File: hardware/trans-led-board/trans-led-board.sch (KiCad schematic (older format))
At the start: 4 parts, among them J1 Conn_01x02

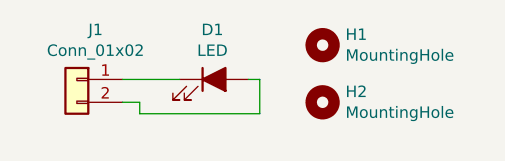
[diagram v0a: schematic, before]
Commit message: Updated transmission LED board design
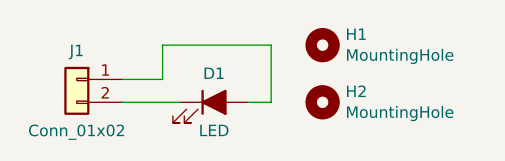
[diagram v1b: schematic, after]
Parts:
- J1: footprint Connector_Wire:SolderWire-0.5sqmm_1x02_P4.6mm_D0.9mm_OD2.1mm -> Connector_JST:JST_SH_SM02B-SRSS-TB_1x02-1MP_P1.00mm_Horizontal; Description (none) -> CONN HEADER SMD R/A 2POS 1MM; Manufacturer (none) -> JST Sales America Inc.; Manufacturer PN (none) -> SM02B-SRSS-TB(LF)(SN); Supplier (none) -> TLC; Supplier PN (none) -> SM02B-SRSS-TB(LF)(SN)
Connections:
- net at D1.1 (K): now also J1.2 (Pin_2); no longer J1.1 (Pin_1)
- net at D1.2 (A): now also J1.1 (Pin_1); no longer J1.2 (Pin_2)
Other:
- moved on the sheet: D1
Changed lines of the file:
@@
 L Device:LED_ALT D1
 U 1 1 609352D1
-P 2575 2050
-F 0 "D1" H 2568 2267 50  0000 C CNN
-F 1 "LED" H 2568 2176 50  0000 C CNN
-F 2 "lib_fp:LED_WL-SWTP-3022" H 2575 2050 50  0001 C CNN
-F 3 "https://katalog.we-online.de/led/datasheet/158302250.pdf" H 2575 2050 50  0001 C CNN
-F 4 "LED WL-SWTP COOL WHT 5000K 2SMD" H 2575 2050 50  0001 C CNN "Description"
-F 5 "Würth Elektronik" H 2575 2050 50  0001 C CNN "Manufacturer"
-F 6 "158302250" H 2575 2050 50  0001 C CNN "Manufacturer PN"
-F 7 "Digi-Key" H 2575 2050 50  0001 C CNN "Supplier"
-F 8 "732-5666-1-ND" H 2575 2050 50  0001 C CNN "Supplier PN"
-	1    2575 2050
+P 2575 2150
+F 0 "D1" H 2575 2275 50  0000 C CNN
+F 1 "LED" H 2575 2025 50  0000 C CNN
+F 2 "lib_fp:LED_WL-SWTP-3022" H 2575 2150 50  0001 C CNN
+F 3 "https://katalog.we-online.de/led/datasheet/158302250.pdf" H 2575 2150 50  0001 C CNN
+F 4 "LED WL-SWTP COOL WHT 5000K 2SMD" H 2575 2150 50  0001 C CNN "Description"
+F 5 "Würth Elektronik" H 2575 2150 50  0001 C CNN "Manufacturer"
+F 6 "158302250" H 2575 2150 50  0001 C CNN "Manufacturer PN"
+F 7 "Digi-Key" H 2575 2150 50  0001 C CNN "Supplier"
+F 8 "732-5666-1-ND" H 2575 2150 50  0001 C CNN "Supplier PN"
+	1    2575 2150
 	1    0    0    -1
 $EndComp
@@
 U 1 1 6093685B
 P 1975 2050
-F 0 "J1" H 1893 2267 50  0000 C CNN
-F 1 "Conn_01x02" H 1893 2176 50  0000 C CNN
-F 2 "Connector_Wire:SolderWire-0.5sqmm_1x02_P4.6mm_D0.9mm_OD2.1mm" H 1975 2050 50  0001 C CNN
-F 3 "~" H 1975 2050 50  0001 C CNN
+F 0 "J1" H 1975 2175 50  0000 C CNN
+F 1 "Conn_01x02" H 1975 1825 50  0000 C CNN
+F 2 "Connector_JST:JST_SH_SM02B-SRSS-TB_1x02-1MP_P1.00mm_Horizontal" H 1975 2050 50  0001 C CNN
+F 3 "https://www.jst-mfg.com/product/pdf/eng/eSH.pdf" H 1975 2050 50  0001 C CNN
+F 4 "CONN HEADER SMD R/A 2POS 1MM" H 1975 2050 50  0001 C CNN "Description"
+F 5 "JST Sales America Inc." H 1975 2050 50  0001 C CNN "Manufacturer"
+F 6 "SM02B-SRSS-TB(LF)(SN)" H 1975 2050 50  0001 C CNN "Manufacturer PN"
+F 7 "TLC" H 1975 2050 50  0001 C CNN "Supplier"
+F 8 "SM02B-SRSS-TB(LF)(SN)" H 1975 2050 50  0001 C CNN "Supplier PN"
 	1    1975 2050
 	-1   0    0    -1
 $EndComp
 Wire Wire Line
-	2425 2050 2175 2050
-Wire Wire Line
-	2725 2050 2775 2050
-Wire Wire Line
-	2775 2050 2775 2200
-Wire Wire Line
-	2775 2200 2250 2200
-Wire Wire Line
-	2250 2200 2250 2150
-Wire Wire Line
-	2250 2150 2175 2150
+	2425 2150 2175 2150
 $Comp
 L Mechanical:MountingHole H1
@@
 	1    0    0    -1
 $EndComp
+Wire Wire Line
+	2175 2050 2350 2050
+Wire Wire Line
+	2350 2050 2350 1900
+Wire Wire Line
+	2350 1900 2825 1900
+Wire Wire Line
+	2825 1900 2825 2150
+Wire Wire Line
+	2825 2150 2725 2150
 $EndSCHEMATC

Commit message: Transmission LED board revision B update
This change is to test adding a substantial thermal pad around the LED,
to see if it has any measurable effect on the brightness drop.

If the test is successful, a similar footprint change will likely be
made to the main PCB for its next revision. If the test is unsuccessful,
this revision may simply be rolled back and forgotten about.
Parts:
- D1: footprint lib_fp:LED_WL-SWTP-3022 -> lib_fp:LED_WL-SWTP-3022-PAD
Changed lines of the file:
@@
 Sheet 1 1
 Title "Printalyzer Densitometer - Transmission LED Board"
-Date "2021-06-15"
-Rev "A"
+Date "2021-10-06"
+Rev "B"
 Comp "Dektronics"
 Comment1 "Derek Konigsberg"
@@
 F 0 "D1" H 2575 2275 50  0000 C CNN
 F 1 "LED" H 2575 2025 50  0000 C CNN
-F 2 "lib_fp:LED_WL-SWTP-3022" H 2575 2150 50  0001 C CNN
+F 2 "lib_fp:LED_WL-SWTP-3022-PAD" H 2575 2150 50  0001 C CNN
 F 3 "https://katalog.we-online.de/led/datasheet/158302250.pdf" H 2575 2150 50  0001 C CNN
 F 4 "LED WL-SWTP COOL WHT 5000K 2SMD" H 2575 2150 50  0001 C CNN "Description"

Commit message: Update LED footprints for thermal properties
Fixes naming convention of thermally-enhanced LED footprints to be
closer to the KiCad convention, and separates into two versions. One
with thermal vias and one without.

Updated transmission board metadata to referene the correct new
footprint name.

Updated main board to use the new version of the new footprint without
thermal vias.

Fixes #22
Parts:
- D1: footprint lib_fp:LED_WL-SWTP-3022-PAD -> lib_fp:LED_WL-SWTP-3022-1MP_ThermalVias
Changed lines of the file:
@@
 F 0 "D1" H 2575 2275 50  0000 C CNN
 F 1 "LED" H 2575 2025 50  0000 C CNN
-F 2 "lib_fp:LED_WL-SWTP-3022-PAD" H 2575 2150 50  0001 C CNN
+F 2 "lib_fp:LED_WL-SWTP-3022-1MP_ThermalVias" H 2575 2150 50  0001 C CNN
 F 3 "https://katalog.we-online.de/led/datasheet/158302250.pdf" H 2575 2150 50  0001 C CNN
 F 4 "LED WL-SWTP COOL WHT 5000K 2SMD" H 2575 2150 50  0001 C CNN "Description"

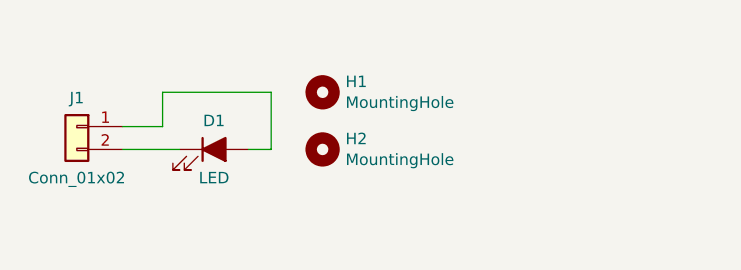
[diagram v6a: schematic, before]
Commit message: Updated transmission LED footprint and added fiducials
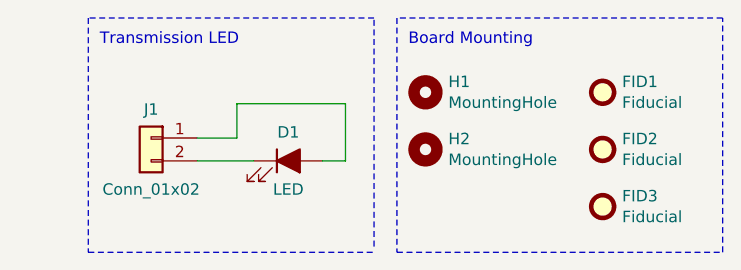
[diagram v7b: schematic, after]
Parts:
- added FID1, FID2, FID3: Fiducial, Fiducial:Fiducial_1mm_Mask2mm, symbol Mechanical:Fiducial
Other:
- note added: "Board Mounting"
- note added: "Transmission LED"
- moved on the sheet: D1, H1, H2, J1
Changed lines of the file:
@@
 Sheet 1 1
 Title "Printalyzer Densitometer - Transmission LED Board"
-Date "2021-10-06"
-Rev "B"
+Date "2021-??-??"
+Rev "C*"
 Comp "Dektronics, Inc."
 Comment1 "Derek Konigsberg <dkonigsberg@dektronics.com>"
@@
 L Device:LED_ALT D1
 U 1 1 609352D1
-P 2575 2150
-F 0 "D1" H 2575 2275 50  0000 C CNN
-F 1 "LED" H 2575 2025 50  0000 C CNN
-F 2 "lib_fp:LED_WL-SWTP-3022-1MP_ThermalVias" H 2575 2150 50  0001 C CNN
-F 3 "https://katalog.we-online.de/led/datasheet/158302250.pdf" H 2575 2150 50  0001 C CNN
-F 4 "LED WL-SWTP COOL WHT 5000K 2SMD" H 2575 2150 50  0001 C CNN "Description"
-F 5 "Würth Elektronik" H 2575 2150 50  0001 C CNN "Manufacturer"
-F 6 "158302250" H 2575 2150 50  0001 C CNN "Manufacturer PN"
-F 7 "Digi-Key" H 2575 2150 50  0001 C CNN "Supplier"
-F 8 "732-5666-1-ND" H 2575 2150 50  0001 C CNN "Supplier PN"
-	1    2575 2150
+P 2900 2200
+F 0 "D1" H 2900 2325 50  0000 C CNN
+F 1 "LED" H 2900 2075 50  0000 C CNN
+F 2 "lib_fp:LED_WL-SWTP-3022-1MP_ThermalVias" H 2900 2200 50  0001 C CNN
+F 3 "https://katalog.we-online.de/led/datasheet/158302250.pdf" H 2900 2200 50  0001 C CNN
+F 4 "LED WL-SWTP COOL WHT 5000K 2SMD" H 2900 2200 50  0001 C CNN "Description"
+F 5 "Würth Elektronik" H 2900 2200 50  0001 C CNN "Manufacturer"
+F 6 "158302250" H 2900 2200 50  0001 C CNN "Manufacturer PN"
+F 7 "Digi-Key" H 2900 2200 50  0001 C CNN "Supplier"
+F 8 "732-5666-1-ND" H 2900 2200 50  0001 C CNN "Supplier PN"
+	1    2900 2200
 	1    0    0    -1
 $EndComp
@@
 L Connector_Generic:Conn_01x02 J1
 U 1 1 6093685B
-P 1975 2050
-F 0 "J1" H 1975 2175 50  0000 C CNN
-F 1 "Conn_01x02" H 1975 1825 50  0000 C CNN
-F 2 "Connector_JST:JST_SH_SM02B-SRSS-TB_1x02-1MP_P1.00mm_Horizontal" H 1975 2050 50  0001 C CNN
-F 3 "https://www.jst-mfg.com/product/pdf/eng/eSH.pdf" H 1975 2050 50  0001 C CNN
-F 4 "CONN HEADER SMD R/A 2POS 1MM" H 1975 2050 50  0001 C CNN "Description"
-F 5 "JST Sales America Inc." H 1975 2050 50  0001 C CNN "Manufacturer"
-F 6 "SM02B-SRSS-TB(LF)(SN)" H 1975 2050 50  0001 C CNN "Manufacturer PN"
-F 7 "TLC" H 1975 2050 50  0001 C CNN "Supplier"
-F 8 "SM02B-SRSS-TB(LF)(SN)" H 1975 2050 50  0001 C CNN "Supplier PN"
-	1    1975 2050
+P 2300 2100
+F 0 "J1" H 2300 2225 50  0000 C CNN
+F 1 "Conn_01x02" H 2300 1875 50  0000 C CNN
+F 2 "Connector_JST:JST_SH_SM02B-SRSS-TB_1x02-1MP_P1.00mm_Horizontal" H 2300 2100 50  0001 C CNN
+F 3 "https://www.jst-mfg.com/product/pdf/eng/eSH.pdf" H 2300 2100 50  0001 C CNN
+F 4 "CONN HEADER SMD R/A 2POS 1MM" H 2300 2100 50  0001 C CNN "Description"
+F 5 "JST Sales America Inc." H 2300 2100 50  0001 C CNN "Manufacturer"
+F 6 "SM02B-SRSS-TB(LF)(SN)" H 2300 2100 50  0001 C CNN "Manufacturer PN"
+F 7 "TLC" H 2300 2100 50  0001 C CNN "Supplier"
+F 8 "SM02B-SRSS-TB(LF)(SN)" H 2300 2100 50  0001 C CNN "Supplier PN"
+	1    2300 2100
 	-1   0    0    -1
 $EndComp
 Wire Wire Line
-	2425 2150 2175 2150
+	2750 2200 2500 2200
+$Comp
+L Mechanical:MountingHole H2
+U 1 1 6093F399
+P 3500 2150
+F 0 "H2" H 3600 2196 50  0000 L CNN
+F 1 "MountingHole" H 3600 2105 50  0000 L CNN
+F 2 "MountingHole:MountingHole_2.2mm_M2" H 3500 2150 50  0001 C CNN
+F 3 "~" H 3500 2150 50  0001 C CNN
+	1    3500 2150
+	1    0    0    -1
+$EndComp
+Wire Wire Line
+	2500 2100 2675 2100
+Wire Wire Line
+	2675 2100 2675 1950
+Wire Wire Line
+	2675 1950 3150 1950
+Wire Wire Line
+	3150 1950 3150 2200
+Wire Wire Line
+	3150 2200 3050 2200
+$Comp
+L Mechanical:Fiducial FID2
+U 1 1 6195409E
+P 4275 2150
+F 0 "FID2" H 4360 2196 50  0000 L CNN
+F 1 "Fiducial" H 4360 2105 50  0000 L CNN
+F 2 "Fiducial:Fiducial_1mm_Mask2mm" H 4275 2150 50  0001 C CNN
+F 3 "~" H 4275 2150 50  0001 C CNN
+	1    4275 2150
+	1    0    0    -1
+$EndComp
+$Comp
+L Mechanical:Fiducial FID3
+U 1 1 619541E3
+P 4275 2400
+F 0 "FID3" H 4360 2446 50  0000 L CNN
+F 1 "Fiducial" H 4360 2355 50  0000 L CNN
+F 2 "Fiducial:Fiducial_1mm_Mask2mm" H 4275 2400 50  0001 C CNN
+F 3 "~" H 4275 2400 50  0001 C CNN
+	1    4275 2400
+	1    0    0    -1
+$EndComp
+Text Notes 3425 1700 0    50   ~ 0
+Board Mounting
+Text Notes 2075 1700 0    50   ~ 0
+Transmission LED
+$Comp
+L Mechanical:Fiducial FID1
+U 1 1 61953C8F
+P 4275 1900
+F 0 "FID1" H 4360 1946 50  0000 L CNN
+F 1 "Fiducial" H 4360 1855 50  0000 L CNN
+F 2 "Fiducial:Fiducial_1mm_Mask2mm" H 4275 1900 50  0001 C CNN
+F 3 "~" H 4275 1900 50  0001 C CNN
+	1    4275 1900
+	1    0    0    -1
+$EndComp
 $Comp
 L Mechanical:MountingHole H1
 U 1 1 6093E7FB
-P 3050 1900
-F 0 "H1" H 3150 1946 50  0000 L CNN
-F 1 "MountingHole" H 3150 1855 50  0000 L CNN
-F 2 "MountingHole:MountingHole_2.2mm_M2" H 3050 1900 50  0001 C CNN
-F 3 "~" H 3050 1900 50  0001 C CNN
-	1    3050 1900
+P 3500 1900
+F 0 "H1" H 3600 1946 50  0000 L CNN
+F 1 "MountingHole" H 3600 1855 50  0000 L CNN
+F 2 "MountingHole:MountingHole_2.2mm_M2" H 3500 1900 50  0001 C CNN
+F 3 "~" H 3500 1900 50  0001 C CNN
+	1    3500 1900
 	1    0    0    -1
 $EndComp
-$Comp
-L Mechanical:MountingHole H2
-U 1 1 6093F399
-P 3050 2150
-F 0 "H2" H 3150 2196 50  0000 L CNN
-F 1 "MountingHole" H 3150 2105 50  0000 L CNN
-F 2 "MountingHole:MountingHole_2.2mm_M2" H 3050 2150 50  0001 C CNN
-F 3 "~" H 3050 2150 50  0001 C CNN
-	1    3050 2150
-	1    0    0    -1
-$EndComp
-Wire Wire Line
-	2175 2050 2350 2050
-Wire Wire Line
-	2350 2050 2350 1900
-Wire Wire Line
-	2350 1900 2825 1900
-Wire Wire Line
-	2825 1900 2825 2150
-Wire Wire Line
-	2825 2150 2725 2150
+Wire Notes Line
+	3375 1575 3375 2600
+Wire Notes Line
+	3375 2600 4800 2600
+Wire Notes Line
+	4800 2600 4800 1575
+Wire Notes Line
+	4800 1575 3375 1575
+Wire Notes Line
+	2025 1575 2025 2600
+Wire Notes Line
+	2025 2600 3275 2600
+Wire Notes Line
+	3275 2575 3275 1575
+Wire Notes Line
+	3275 1575 2025 1575
 $EndSCHEMATC
